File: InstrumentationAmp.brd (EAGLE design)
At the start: 21 x 23.5 mm, 14 parts, among them IC1 AD623R

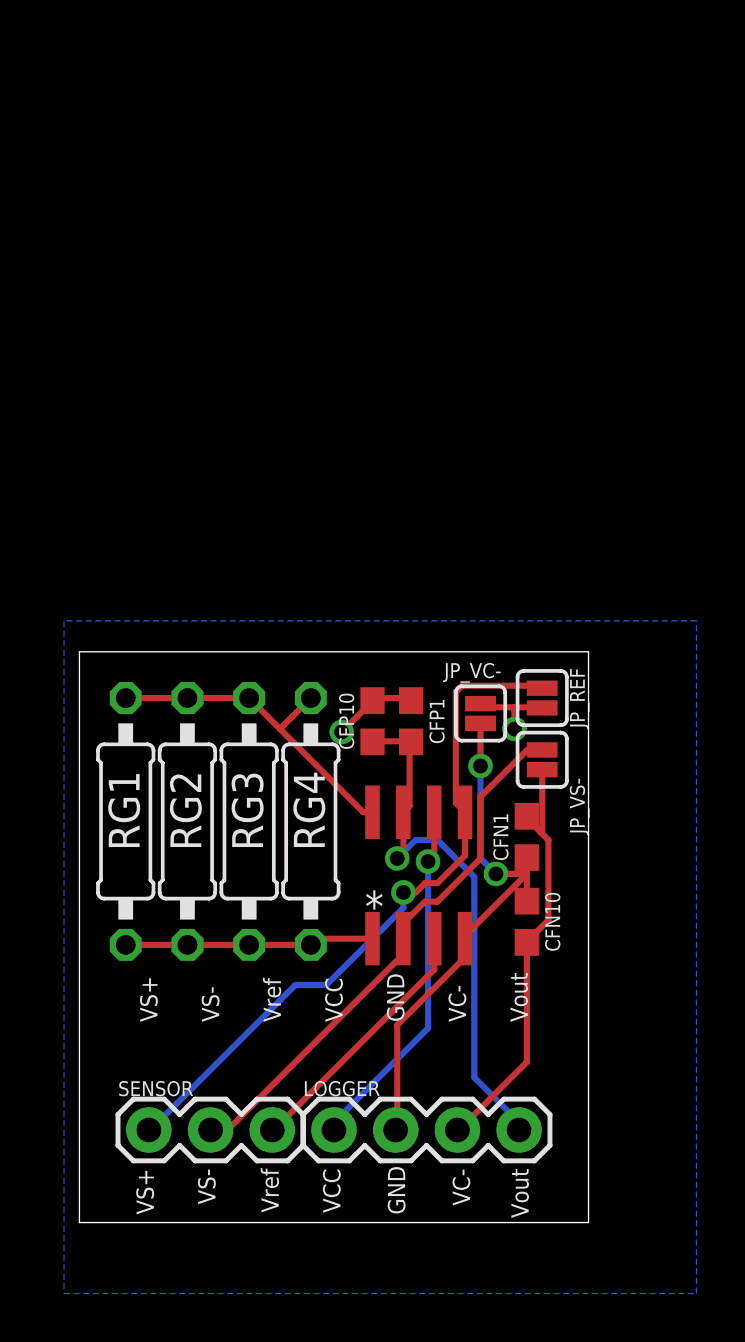
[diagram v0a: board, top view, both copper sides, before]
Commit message: Initial layout of Amp 2.0
Changed schematic to add on board buck-boost converter, mux to control gain, and I2C IO expander to allow gain to be controlled via I2C. Preliminary layout complete, ready for verification
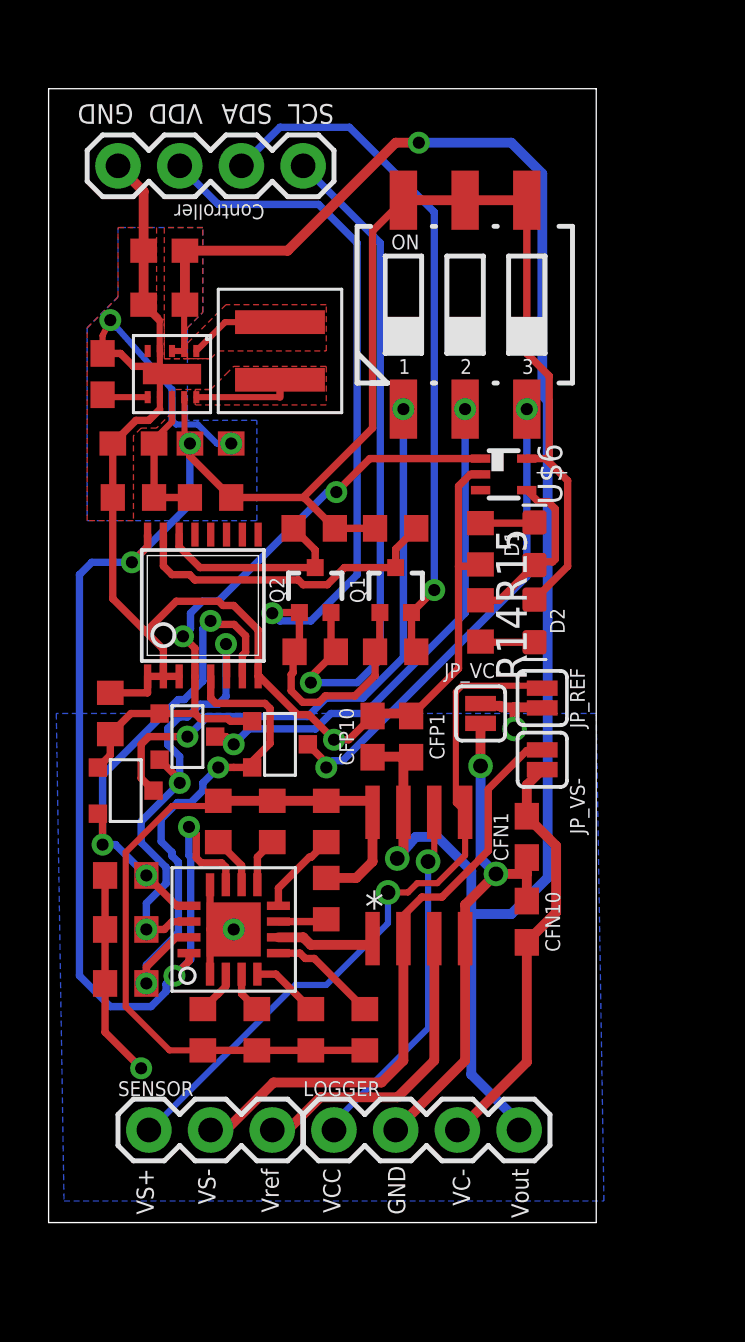
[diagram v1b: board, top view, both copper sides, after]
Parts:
- removed RG1, RG2, RG3, RG4: (no value), resistor:0207/10
- added C1: 0.1uF, rcl:C0603
- added C2, C7: 10uF, rcl:C0603
- added C3: 10pF, rcl:C0603
- added C5: 22uF, rcl:C0603
- added D1: GREEN, SparkFun-LED:LED-0603
- added D2: BLUE, SparkFun-LED:LED-0603
- added J1: (no value), SparkFun-Connectors:1X04
- added Q1, Q2: 310mA/60V/1.6Ω, SparkFun-DiscreteSemi:SOT323
- added R10, R11, R12, R14, R15, R16, R17, R18, R19, R5, R6, R7, R8, R9: (no value), rcl:R0603
- added R13, R2, R3, R4: 10k, rcl:R0603
- added R20: 143k, rcl:R0603
- added R21: 953k, rcl:R0603
- added S1: 219-03, switch-dil:CTS-219-03
- added U$1: MAX4638, Custom:TQFN16
- added U$2: TCA9534A, Custom:TSSOP16
- added U$3, U$4, U$5: FDN358P, Custom:SSOT-3
- added U$6: MIC842, Custom:DCK_R-PDSO-G5
- added U$7: TPS63061, Custom:WSON-10
- added U$8: 1uH, Custom:WE-MAIA(4.1X4.1)
- moved CFP1 0.63 mm to (13.7, 20.0)
- moved CFP10 0.63 mm to (12.1, 20.0)
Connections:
- removed net RG-A: IC1.1, RG1.2, RG2.2, RG3.2, RG4.2
- removed net RG-B: IC1.8, RG1.1, RG2.1, RG3.1, RG4.1
- new net 5V: C5.1, D2.A, R18.2, R19.2, R21.2, S1.4, S1.5, S1.6, U$1.11, U$1.16, U$2.16, U$6.5, U$7.P$9
- new net INT: U$2.13
- new net N$1: U$7.P$10, U$8.P$2
- new net N$11: R7.2, U$1.4
- new net N$12: R8.2, U$1.5
- new net N$13: R9.2, U$1.10
- new net N$14: R10.2, U$1.9
- new net N$15: R11.2, U$1.8
- new net N$16: R12.2, U$1.7
- new net N$17: D1.C, R15.1
- new net N$18: D1.A, R14.1, U$6.4
- new net N$19: C3.1, R20.2, R21.1, U$7.P$8
- new net N$2: U$7.P$1, U$8.P$1
- new net N$3: D2.C, R14.2
- new net N$4: S1.2, U$4.3
- new net N$5: C1.1, U$7.P$6
- new net N$6: S1.3, U$5.3
- new net N$7: S1.1, U$3.3
- new net N$8: R5.2, U$1.2
- new net N$9: R6.2, U$1.3
- new net R_GAIN+: IC1.1, U$1.6
- new net R_GAIN-: IC1.8, R10.1, R11.1, R12.1, R5.1, R6.1, R7.1, R8.1, R9.1
- new net S1: R4.2, U$1.15, U$2.5, U$5.2
- new net S2: R2.2, U$1.14, U$2.6, U$4.2
- new net S3: R3.2, U$1.13, U$2.7, U$3.2
- new net SCL: Q2.3, R19.1, U$2.14
- new net SCL_OUT: J1.4, Q2.2, R17.1
- new net SDA: Q1.3, R18.1, U$2.15
- new net SDA_OUT: J1.3, Q1.2, R16.1
- new net SW_G: R13.2, U$2.4, U$3.1, U$4.1, U$5.1, U$6.1
- new net V_LOGIC: J1.2, Q1.1, Q2.1, R16.2, R17.2
- net GND: now also C1.2, C2.2, C3.2, C5.2, C7.2, J1.1, R13.1, R15.2, R2.1, R20.1, R3.1, R4.1, U$1.1, U$1.12, U$1.17, U$2.1, U$2.2, U$2.3, U$2.8, U$6.2, U$7.P$11, U$7.P$4, U$7.P$7
- net VCC: now also C2.1, C7.1, U$7.P$2, U$7.P$3
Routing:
- net 5V: track 0.00 -> 91.6 mm, vias 0 -> 4
- net GND: track 24.6 -> 103.1 mm, vias 2 -> 6
- net VCC: track 22.0 -> 76.6 mm, vias 1 -> 2
- net V_LOGIC: track 0.00 -> 38.2 mm, vias 0 -> 1
- net R_GAIN-: track 0.00 -> 32.7 mm
- net SDA_OUT: track 0.00 -> 28.7 mm, vias 0 -> 1
- net SCL_OUT: track 0.00 -> 28.4 mm, vias 0 -> 1
- net SW_G: track 0.00 -> 26.9 mm, vias 0 -> 2
- net N$7: track 0.00 -> 24.6 mm, vias 0 -> 2
- net S1: track 0.00 -> 21.6 mm, vias 0 -> 2
- net N$4: track 0.00 -> 21.1 mm, vias 0 -> 2
- net S3: track 0.00 -> 20.7 mm, vias 0 -> 3
- net S2: track 0.00 -> 20.0 mm, vias 0 -> 3
- net N$6: track 0.00 -> 19.7 mm, vias 0 -> 2
- net RG-B: track 13.9 -> 0.00 mm
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- added copper zone on layer 1, net GND
- added copper zone on layer 1, net N$1
- added copper zone on layer 1, net N$2
- added copper zone on layer 1, net VCC
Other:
- board size 21 x 23.5 mm -> 22.5 x 46.7 mm
- board text added: "Controller"
- board text added: "SCL"
- board text added: "SDA"
- board text added: "VDD"

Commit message: Fixed spacing for screw terminals, ready for final check
Moved the screw terminals and silk screen to support screw terminal sizes, fixed one air wire on board layout, ready for final check before ordering
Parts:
- moved LOGGER 2.29 mm to (10.5, 1.52)
- moved SENSOR 2.29 mm to (2.86, 1.52)
- moved J1 1.27 mm to (1.59, 44.8)
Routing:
- net GND: track 103.1 -> 111.1 mm
- net VREF: track 29.1 -> 31.3 mm
- net VCC: track 76.6 -> 78.8 mm
- net VOUT: track 14.8 -> 17.1 mm
- net VNEG: track 22.6 -> 24.8 mm
- net VS-: track 25.8 -> 27.7 mm
- net VS+: track 12.9 -> 14.8 mm
- net SCL_OUT: track 28.4 -> 29.7 mm
- net SDA_OUT: track 28.7 -> 30.0 mm
- net V_LOGIC: track 38.2 -> 38.7 mm
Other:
- board size 22.5 x 46.7 mm -> 22.5 x 49.6 mm

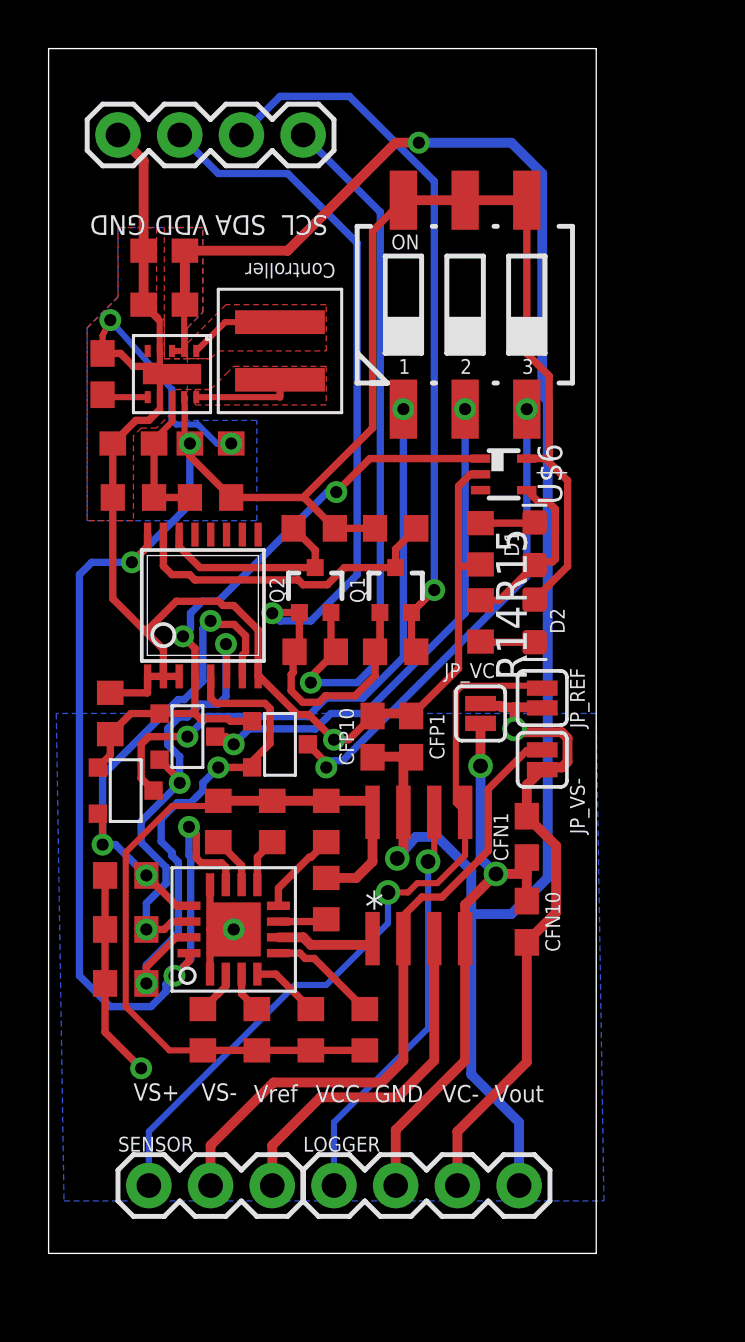
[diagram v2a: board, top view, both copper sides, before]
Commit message: Made Edits from 1st round of board testing
Flipped direciton of PFETs, fixed switch mode regulator package, changed capacitor sizes, chained set resistor values, etc. Verification still required that all changes are made
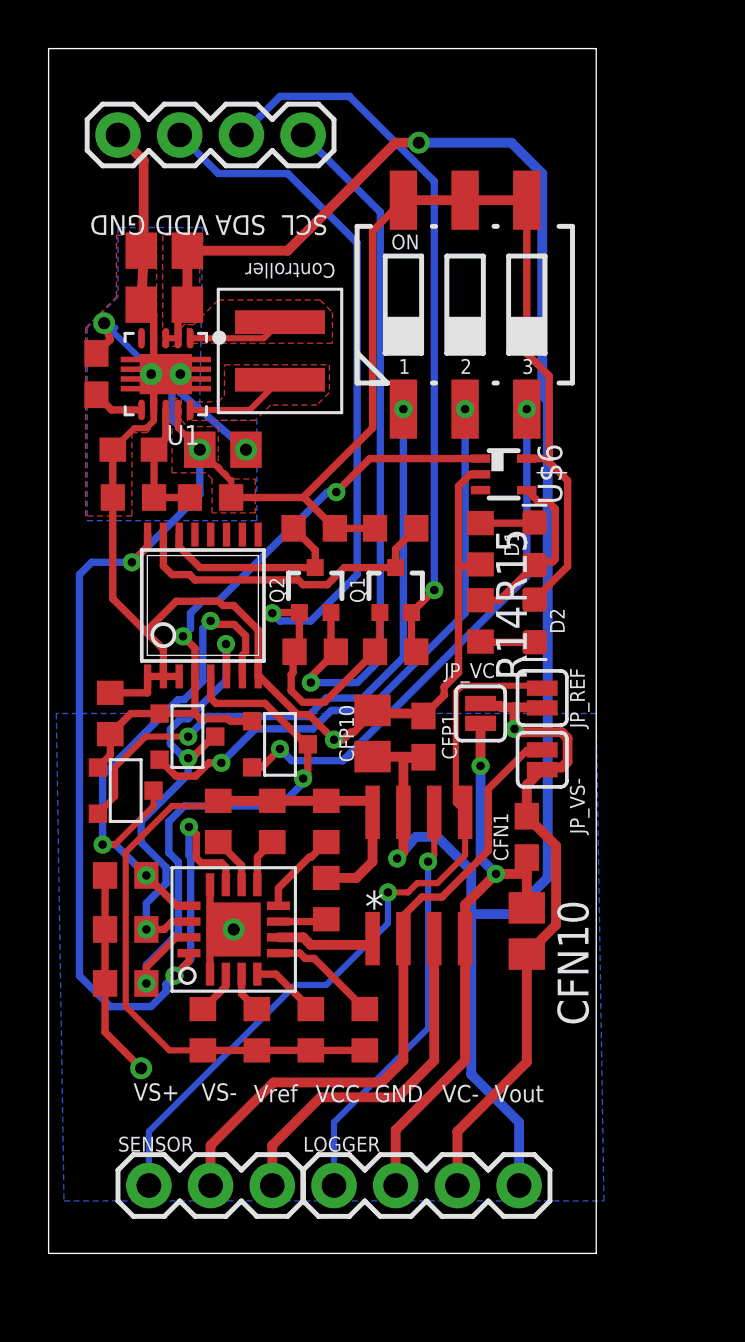
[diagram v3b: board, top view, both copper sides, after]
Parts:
- removed U$7: TPS63061, Custom:WSON-10
- added U1: (no value), bschulz:PWSON-N10
- C2, C5, C7: device rcl:C0603 -> bschulz:C0805
- CFN10, CFP10: device SparkFun-Capacitors:0603 -> bschulz:C0805
- R20: value 143k -> 111k
- R21: value 953k -> 1M
- moved C5 0.57 mm to (5.91, 31.8)
- moved CFP1 0.51 mm to (14.2, 20.0)
- moved CFN10 0.38 mm to (18.4, 12.0)
- moved C3 0.25 mm to (2.22, 31.8)
- moved C1 0.25 mm to (0.70, 34.9)
- moved CFP10 0.13 mm to (12.1, 20.1)
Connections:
- removed net N$2: U$7.P$1, U$8.P$1
- removed net N$4: S1.2, U$4.3
- new net N$20: U$8.P$2, U1.10
- new net N$23: C1.1, U1.6
- net 5V: now also U1.9; no longer U$7.P$9
- net GND: now also U1.4, U1.7, U1.THERMAL@1, U1.THERMAL@10, U1.THERMAL@11, U1.THERMAL@12, U1.THERMAL@13, U1.THERMAL@14, U1.THERMAL@5, U1.THERMAL@6, U1.THERMAL@7, U1.THERMAL@8, U1.THERMAL@9; no longer U$7.P$11, U$7.P$4, U$7.P$7
- net N$1: now also S1.2, U$4.2; no longer U$7.P$10, U$8.P$2
- net N$19: now also U1.8; no longer U$7.P$8
- net N$5: now also U$8.P$1, U1.1; no longer C1.1, U$7.P$6
- net N$6: now also U$5.2; no longer U$5.3
- net N$7: now also U$3.2; no longer U$3.3
- net S1: now also U$5.3; no longer U$5.2
- net S2: now also U$4.3; no longer U$4.2
- net S3: now also U$3.3; no longer U$3.2
- net VCC: now also U1.2, U1.3; no longer U$7.P$2, U$7.P$3
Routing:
- net N$4: track 21.1 -> 0.00 mm, vias 2 -> 0
- net N$1: track 4.16 -> 24.0 mm, vias 0 -> 2
- net N$20: track 0.00 -> 4.21 mm
- net N$2: track 3.94 -> 0.00 mm
- net S1: track 21.6 -> 23.8 mm
- net N$6: track 19.7 -> 21.8 mm
- net N$23: track 0.00 -> 2.12 mm
- net N$5: track 1.90 -> 3.97 mm
- net S3: track 20.7 -> 22.6 mm
- net N$7: track 24.6 -> 26.2 mm
- net VCC: track 78.8 -> 80.0 mm
- net N$19: track 5.91 -> 5.28 mm
- net V_LOGIC: track 38.7 -> 38.1 mm
- added copper zone on layer 1, net 5V
- added copper zone on layer 1, net N$20
- added copper zone on layer 1, net N$5
- removed copper zone on layer 1, net N$1
- removed copper zone on layer 1, net N$2

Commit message: Fixed some DRC errors, added to ground plane
Made additions to power ground plane, fixed releveant DRC errors, ready for checking
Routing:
- net GND: track 110.9 -> 132.8 mm
